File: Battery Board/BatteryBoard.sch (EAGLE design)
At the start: 33 parts, among them IC1 TPS63060DSCT, J0 1725656, J1 1725669, J2 UJ2-MIBH2-4-SMT-TR, J3 MPTC-02-16-02-6.30-XX-X-V, J4 JSTPH2, J5 MPTC-02-04-02-6.30-XX-X-V-LC, Q1 IAUC60N04S6L030HATMA1, U0 STM32L031K4U6, U1 MCP73831T-2ATI_OT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

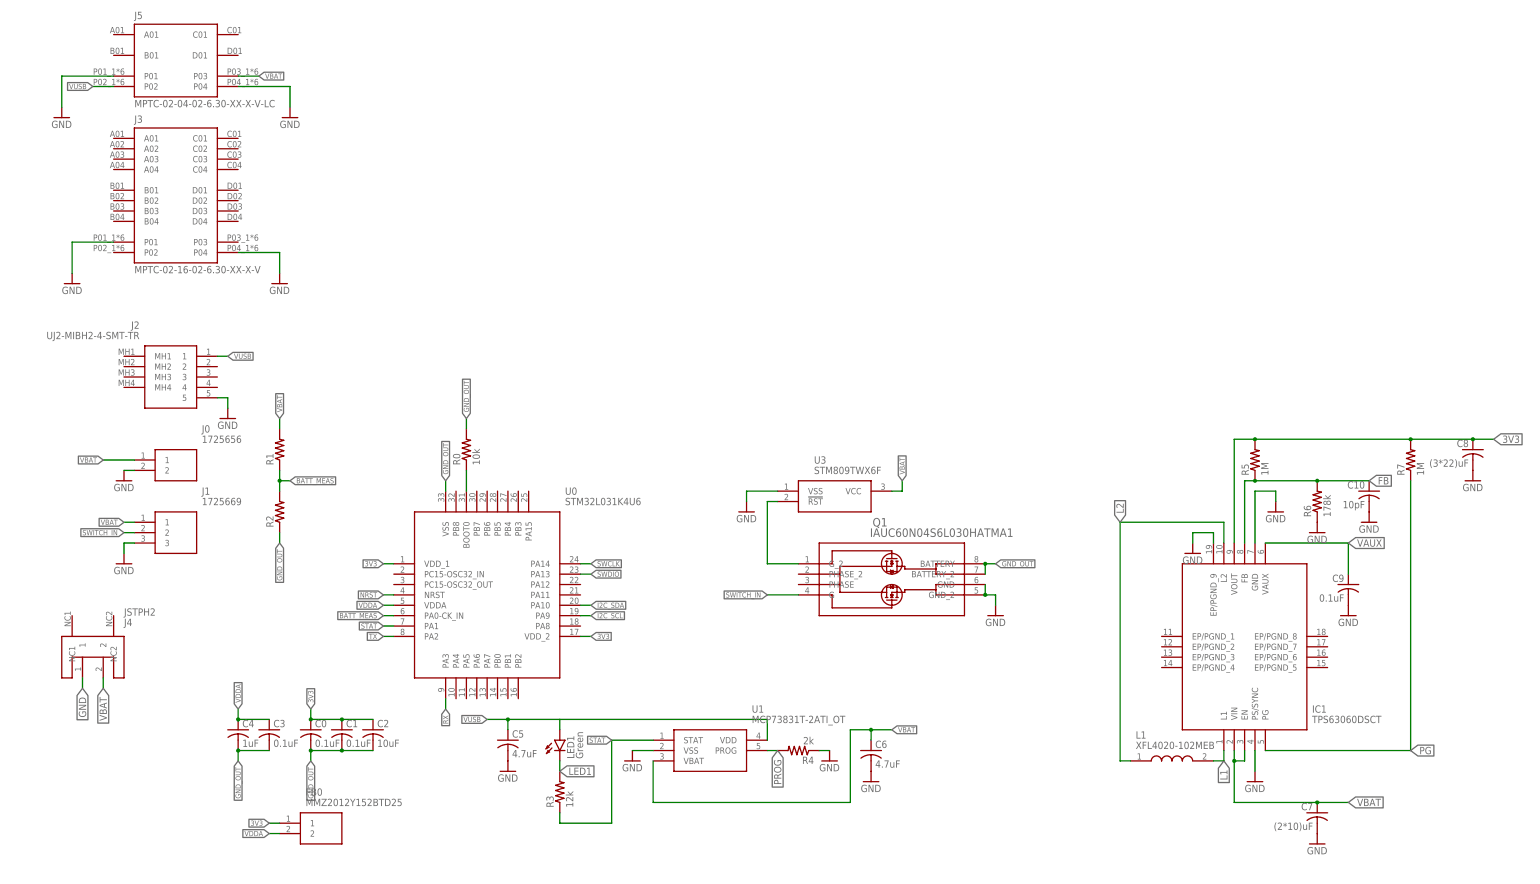
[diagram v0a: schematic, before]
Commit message: Finished Schematic Pin Connections
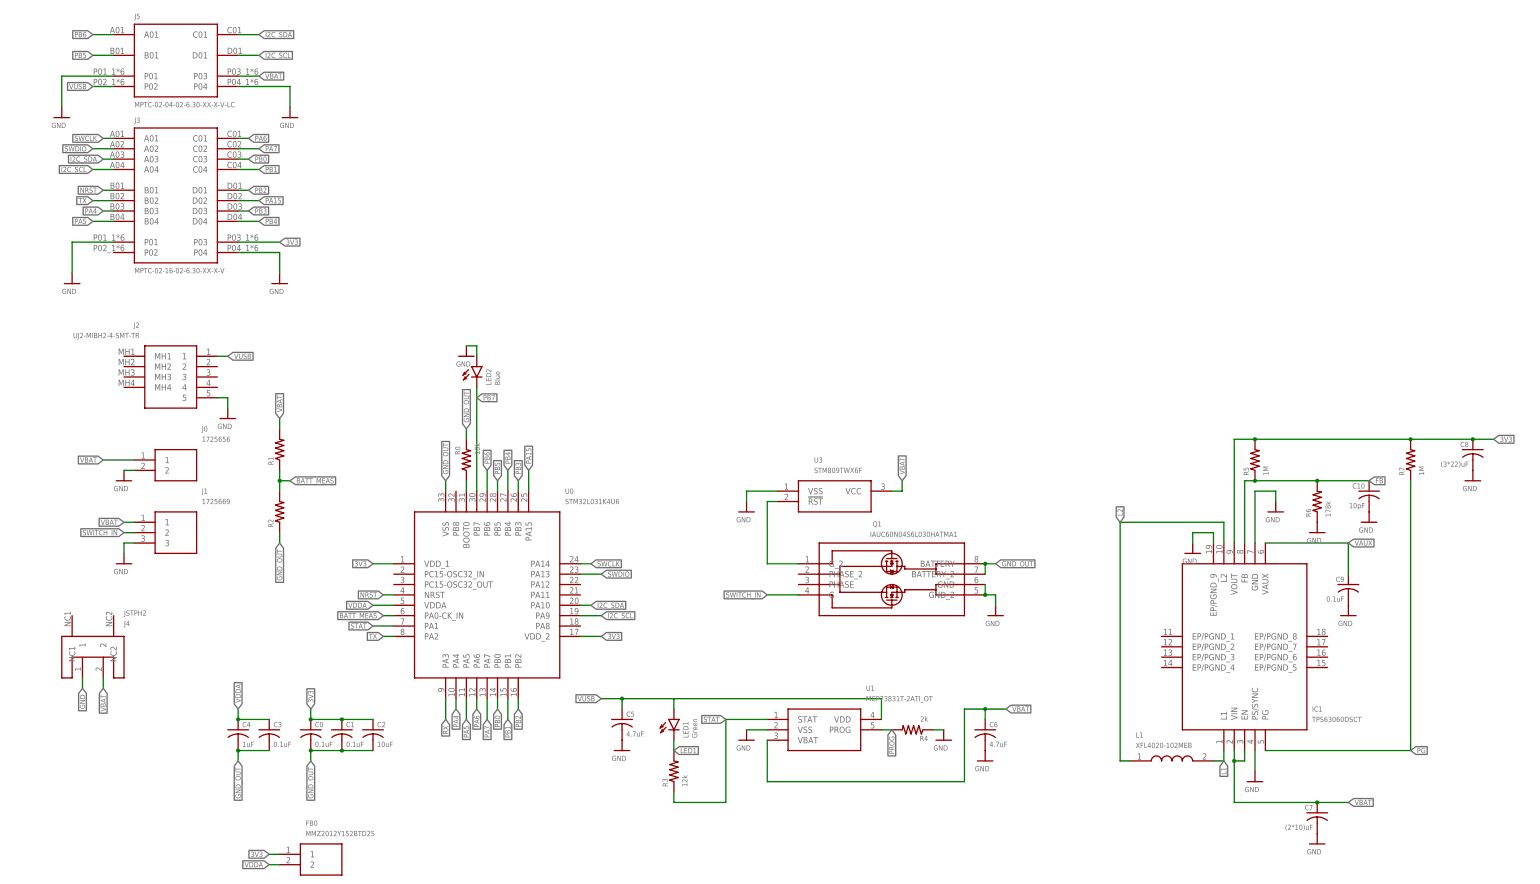
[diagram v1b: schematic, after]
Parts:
- added LED2: Blue, led:LEDCHIP-LED0805
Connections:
- new net PA15: J3.D02, U0.PA15
- new net PA4: J3.B03, U0.PA4
- new net PA5: J3.B04, U0.PA5
- new net PA6: J3.C01, U0.PA6
- new net PA7: J3.C02, U0.PA7
- new net PB0: J3.C03, U0.PB0
- new net PB1: J3.C04, U0.PB1
- new net PB2: J3.D01, U0.PB2
- new net PB3: J3.D03, U0.PB3
- new net PB4: J3.D04, U0.PB4
- new net PB5: J5.B01, U0.PB5
- new net PB6: J5.A01, U0.PB6
- new net PB7: LED2.C, U0.PB7
- net 3V3: now also J3.P03
- net GND: now also LED2.A
- net I2C_SCL: now also J3.A04, J5.D01
- net I2C_SDA: now also J3.A03, J5.C01
- net NRST: now also J3.B01
- net SWCLK: now also J3.A01
- net SWDIO: now also J3.A02
- net TX: now also J3.B02
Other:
- moved on the sheet: C5, C6, FB0, LED1, R0, R3, R4, U1
